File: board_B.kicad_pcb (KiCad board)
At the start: 2 copper layers, 19.1 x 100 mm, 61 parts, among them J1 MIDI In, J2 EuroPower10_THT, J3 Pitch, J4 Clock, J5 Clock2, J6 Gate, J7 MIDI Through, J8 CC, J9 Conn_02x04_Odd_Even, U1 6N137, U3 TL072, U4 TL072

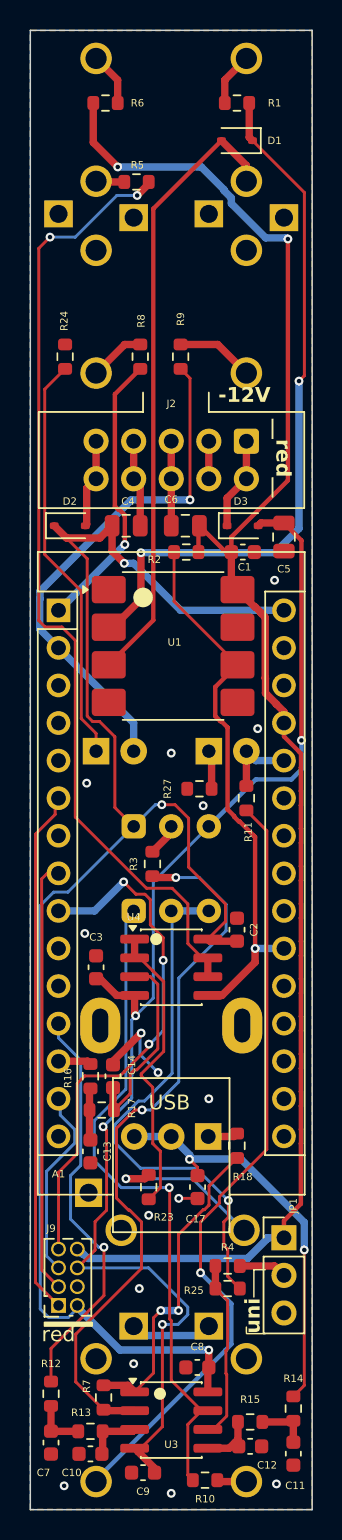
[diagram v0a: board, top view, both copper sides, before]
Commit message: add rev 2 and rev 3, now with correct trs midi A
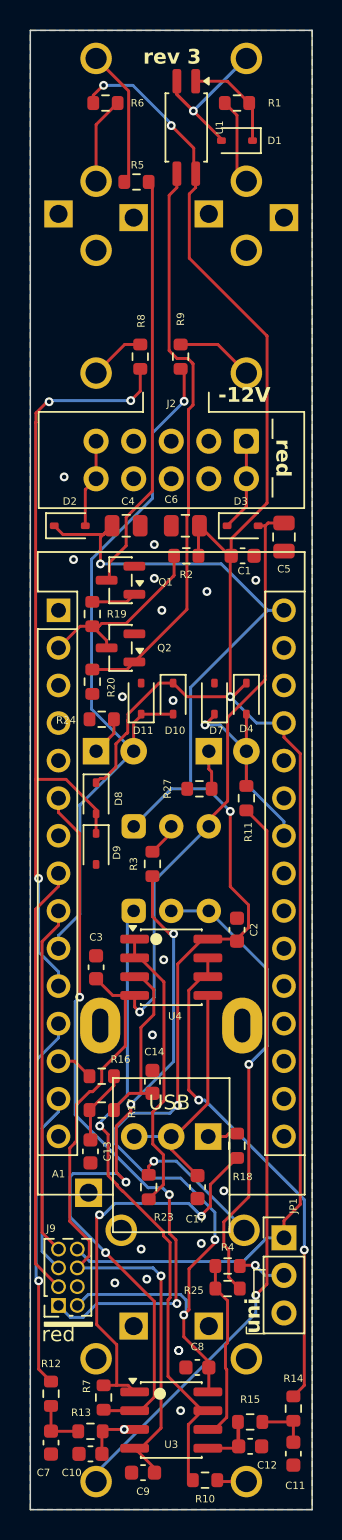
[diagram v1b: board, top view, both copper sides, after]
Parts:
- added D10: 1N5819WS, Diode_SMD:D_SOD-323, F.Cu at (148.6, 65.2)
- added D11: 1N5819WS, Diode_SMD:D_SOD-323, F.Cu at (146.5, 65.2)
- added D4: 1N5819WS, Diode_SMD:D_SOD-323, F.Cu at (153.6, 65.2)
- added D7: 1N5819WS, Diode_SMD:D_SOD-323, F.Cu at (151.4, 65.2)
- added D8: 1N5819WS, Diode_SMD:D_SOD-323, F.Cu at (143.4, 71.9)
- added D9: 1N5819WS, Diode_SMD:D_SOD-323, F.Cu at (143.4, 75.3)
- added Q1: MMBT5551L, Package_TO_SOT_SMD:SOT-23, F.Cu at (145.1, 57.2)
- added Q2: MMBT5551L, Package_TO_SOT_SMD:SOT-23, F.Cu at (145.1, 61.7)
- added R19: 1k, Resistor_SMD:R_0603_1608Metric, F.Cu at (143.2, 59.5)
- added R20: 1k, Resistor_SMD:R_0603_1608Metric, F.Cu at (143.2, 64.0)
- R2: value 10k -> 1k
- U1: value 6N137 -> EL3H7(C)(TA)-G; footprint Package_SO:SOP-8_6.605x9.655mm_P2.54mm -> Package_SO:SSOP-4_4.4x2.6mm_P1.27mm
- moved U1 35.1 mm to (149.5, 26.6), turned to -90 degrees
- moved R24 24.6 mm to (143.8, 66.6), turned to 180 degrees
- moved C14 2.69 mm to (147.2, 91.1)
- moved R16 0.76 mm to (143.8, 90.7), turned to 180 degrees
- moved C1 0.25 mm to (153.3, 55.5)
- moved R2 0.25 mm to (149.5, 55.5)
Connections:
- A1 pad 1: CLOCK -> unconnected-(A1-D1/TX-Pad1)
- A1 pad 10: unconnected-(A1-D7-Pad10) -> CLOCK2
- A1 pad 11: unconnected-(A1-D8-Pad11) -> CLOCK
- A1 pad 2: CLOCK2 -> MIDI_IN
- A1 pad 21: MIDI_IN -> unconnected-(A1-A2-Pad21)
- A1 pad 24: unconnected-(A1-A5-Pad24) -> GATE
- A1 pad 26: GATE -> unconnected-(A1-A7-Pad26)
- C17 pad 1: SLEW_OUT -> Net-(U4B-+)
- J1 pad R: Net-(D1-A) -> Net-(J1-PadR)
- J1 pad S: B_GND -> unconnected-(J1-PadS)
- J1 pad T: Net-(J1-PadT) -> Net-(D1-A)
- R1 pad 1: Net-(J1-PadT) -> Net-(J1-PadR)
- R5 pad 1: Net-(U4B--) -> Net-(Q1-C)
- R5 pad 2: Net-(J7-PadR) -> Net-(J7-PadT)
- R6 pad 2: Net-(J7-PadT) -> Net-(J7-PadR)
- RV5 pad 2: SLEW_OUT -> Net-(U4B-+)
- RV5 pad 3: SLEW_OUT -> Net-(U4B-+)
- U1 pad 1: unconnected-(U1-NC-Pad1) -> Net-(D1-K)
- U1 pad 2: Net-(D1-K) -> Net-(D1-A)
- U1 pad 3: Net-(D1-A) -> Net-(Q2-B)
- U1 pad 4: unconnected-(U1-NC-Pad4) -> B_+5V
- U4 pad 5: MIDI_IN -> Net-(U4B-+)
- U4 pad 6: Net-(U4B--) -> SLEW_OUT
- U4 pad 7: Net-(U4B--) -> SLEW_OUT
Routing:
- net Net-(U4B--): track 65.2 -> 0.00 mm, vias 2 -> 0
- net Net-(D1-K): track 47.9 -> 6.86 mm, vias 2 -> 0
- net Net-(Q2-B): track 0.00 -> 39.0 mm
- net CLOCK: track 19.2 -> 55.1 mm, vias 1 -> 3
- net Net-(D1-A): track 42.0 -> 11.9 mm, vias 0 -> 1
- net Net-(Q1-C): track 0.00 -> 28.3 mm
- net B_GND: track 27.2 -> 0.00 mm, vias 16 -> 19
- net Net-(D5-K): track 27.9 -> 2.66 mm
- net MIDI_IN: track 37.4 -> 13.0 mm, vias 1 -> 0
- net Net-(U4B-+): track 0.00 -> 16.6 mm
- net B_+5V: track 110.0 -> 125.4 mm, vias 2 -> 3
- net CLOCK2: track 35.3 -> 50.0 mm
- net EXP7: track 35.9 -> 23.8 mm, vias 3 -> 0
- net EXP1: track 35.6 -> 47.1 mm, vias 0 -> 3
- net GATE: track 5.15 -> 16.1 mm, vias 0 -> 1
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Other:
- board text added: "rev 3"
